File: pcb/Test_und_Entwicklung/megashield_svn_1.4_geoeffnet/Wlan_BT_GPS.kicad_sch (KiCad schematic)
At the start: 22 parts, among them P44 Wlan, P5 GPS, U10 SN74LVC1T45DBV, U11 Wlan_ESP8266, U13 SN74LVC1T45DBV, U14 SN74LVC1T45DBV, U15 SN74LVC1T45DBV, U16 SN74LVC1T45DBV, U2 Bluetooth_CZ_HC_05, U3 SN74LVC1T45DBV

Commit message: megashield_svn_1.4_geoeffnet
megashield_svn_1.4_geoeffnet
11 Sicherheitskopie alles fertig gezeichnet
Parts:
- C34, C35, C36: Bauform (none) -> Value; Bestelllink (none) -> https://www.reichelt.de/de/en/mlcc-1206-100nf-100v-5--x7r-1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; Bestellnummer (none) -> Value; Bestücken (Assemble) (none) -> JA (YES); Funktion (none) -> X7R 1206 BG 100N MLCC, 1206, 100nF, 100V, 5%; Gehäuseart (none) -> 1206; Hersteller (none) -> Value; Hersteller Bestellnummer (none) -> Value; Technische Daten (none) -> X7R 1206 BG 100N MLCC, 1206, 100nF, 100V, 5%

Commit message: megashield_svn_1.4_geoeffnet
megashield_svn_1.4_geoeffnet
12 Bauteile Links hinzugefügt
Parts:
- JP10, JP11, JP12, JP2, JP4, JP5, JP6, JP7, JP9, P44, P5, U11: Bestücken (Assemble) (none) -> NEIN (NO)
- U10, U13, U14, U15, U16, U3: Bestücken (Assemble) (none) -> JA (YES); Funktion (none) -> Translation - Voltage Levels; Gehäuseart (none) -> SOT-23-6; Technische Daten (none) -> Translation - Voltage Levels
- U2: Bestellnummer Value -> (none); Bestücken (Assemble) (none) -> NEIN (NO); Gehäuseart Value -> (none)

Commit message: megashield_svn_1.4_geoeffnet
megashield_svn_1.4_geoeffnet
16 Puffer Kondensator für ESP 8266 Wlan Modul hinzugefügt
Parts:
- added C38: 22uF / 63V, Zimprich:Elko_vert_11.2x6.3mm_RM2.5_RM5.0, symbol ardumower-mega-shield-svn-rescue:CP_Small-RESCUE-ardumower_mega_shield_svn
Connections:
- net GND: now also C38.2
- net at C35.1, JP6.2, P44.1 (P1)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: now also C38.1

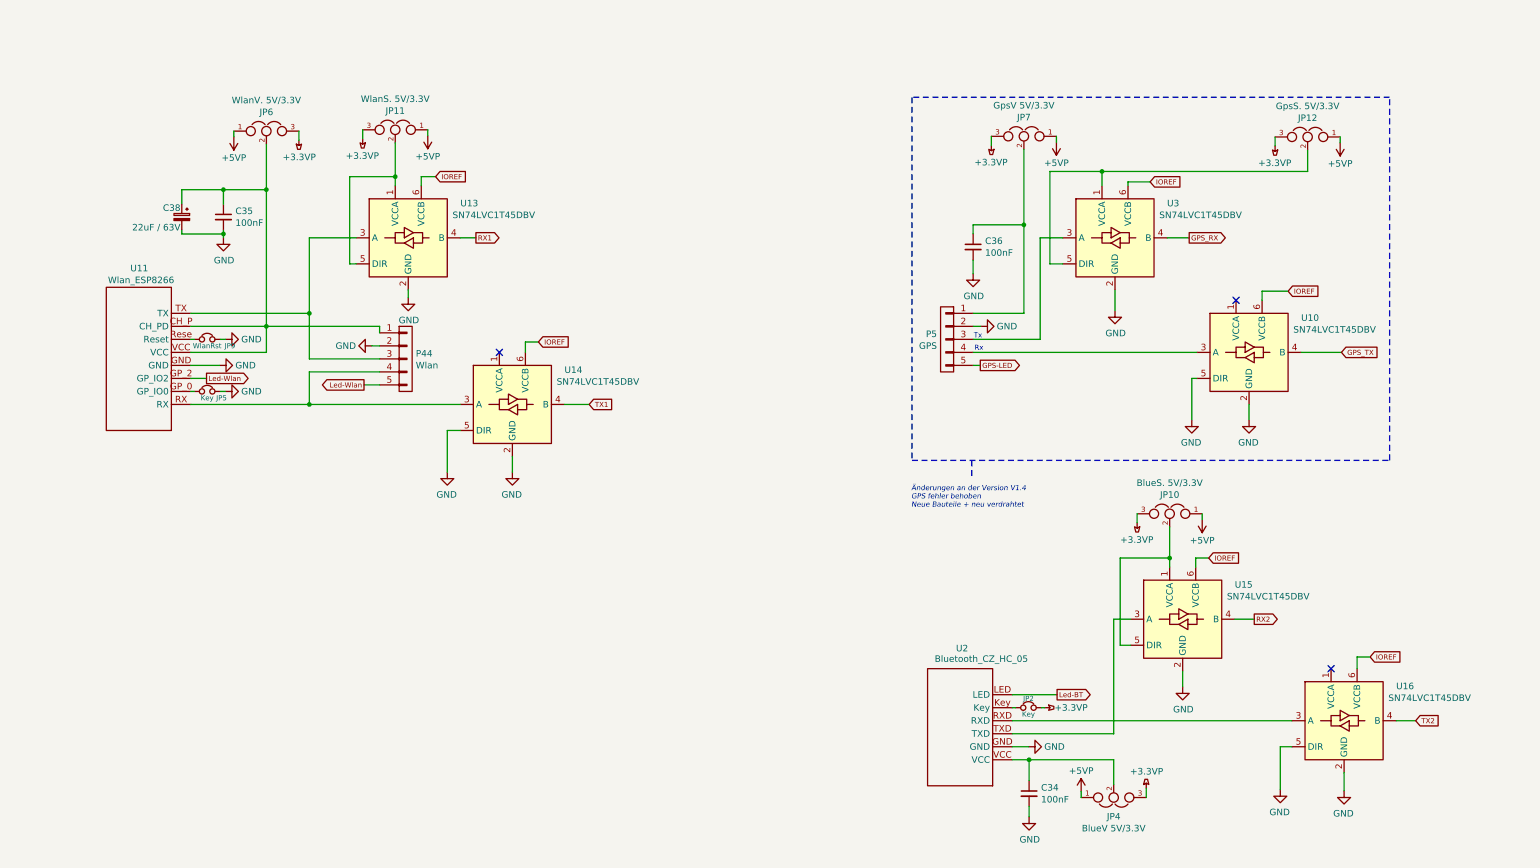
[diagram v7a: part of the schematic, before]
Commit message: megashield_svn_1.4_geoeffnet
21 Verdrahtungfehler bei Levelshifter behoben
VCCA auf den Pegel Jumper gelegt für Wlan, BT
und Gps Glättungskondensatoren hinzugefügt
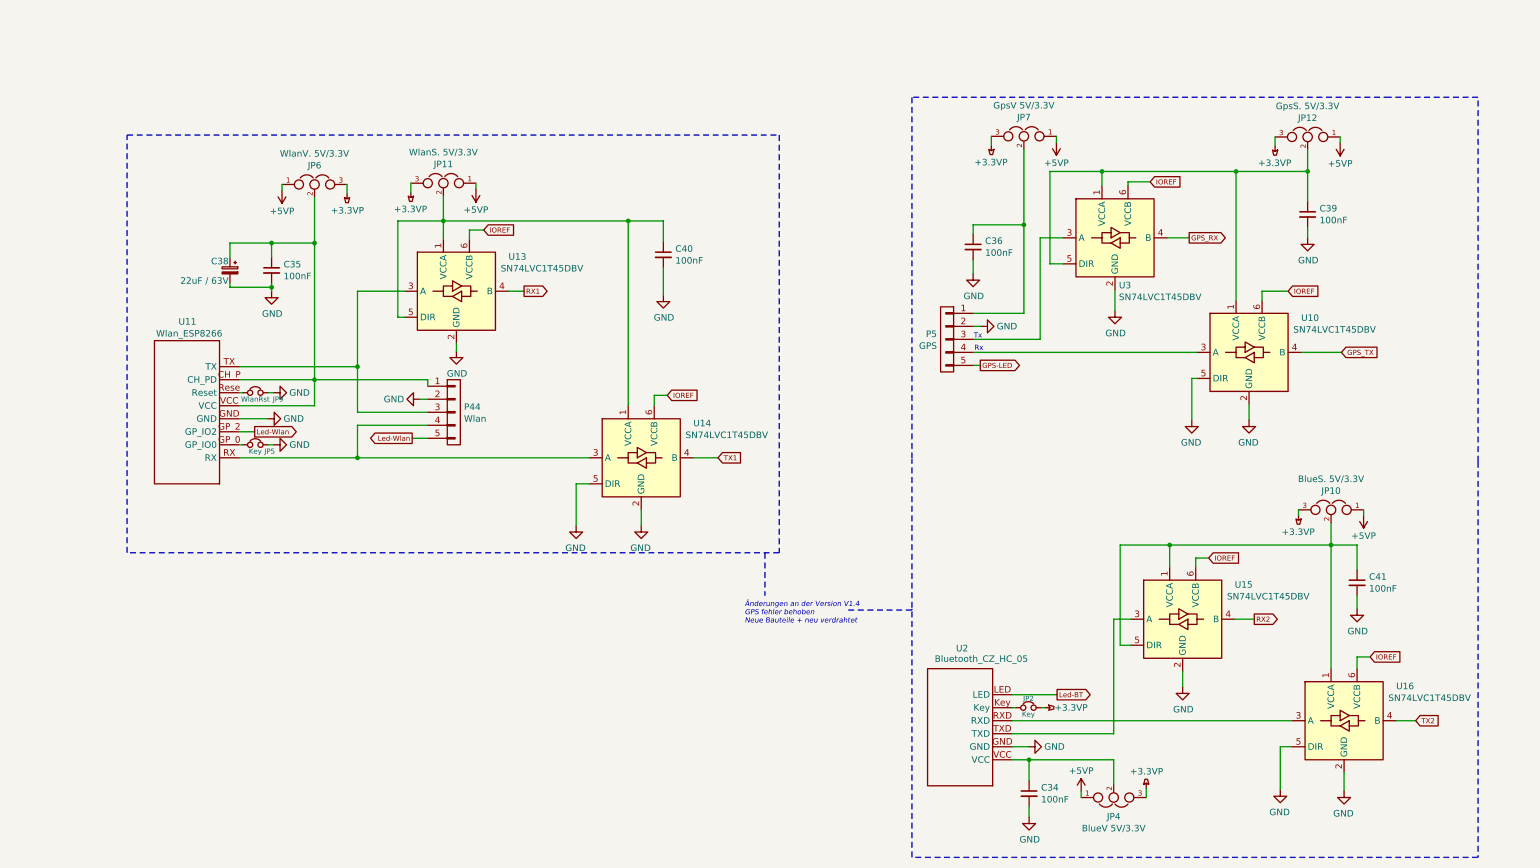
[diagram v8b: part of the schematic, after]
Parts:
- added C39, C40, C41: 100nF, Capacitor_SMD:C_0805_2012Metric, symbol ardumower-mega-shield-svn-rescue:C_Small-RESCUE-ardumower_mega_shield_svn
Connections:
- net GND: now also C39.2, C40.2, C41.2
- net at JP11.2, U13.1 (VCCA), U13.5 (DIR): now also U14.1 (VCCA), C40.1
- net at JP12.2, U3.1 (VCCA), U3.5 (DIR): now also U10.1 (VCCA), C39.1
- net at JP10.2, U15.1 (VCCA), U15.5 (DIR): now also U16.1 (VCCA), C41.1
- no-connect marks 3 -> 0
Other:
- moved on the sheet: C35, C38, JP10, JP11, JP5, JP6, JP9, P44, U11, U13, U14
